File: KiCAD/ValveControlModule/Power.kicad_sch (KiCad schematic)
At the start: 1 part

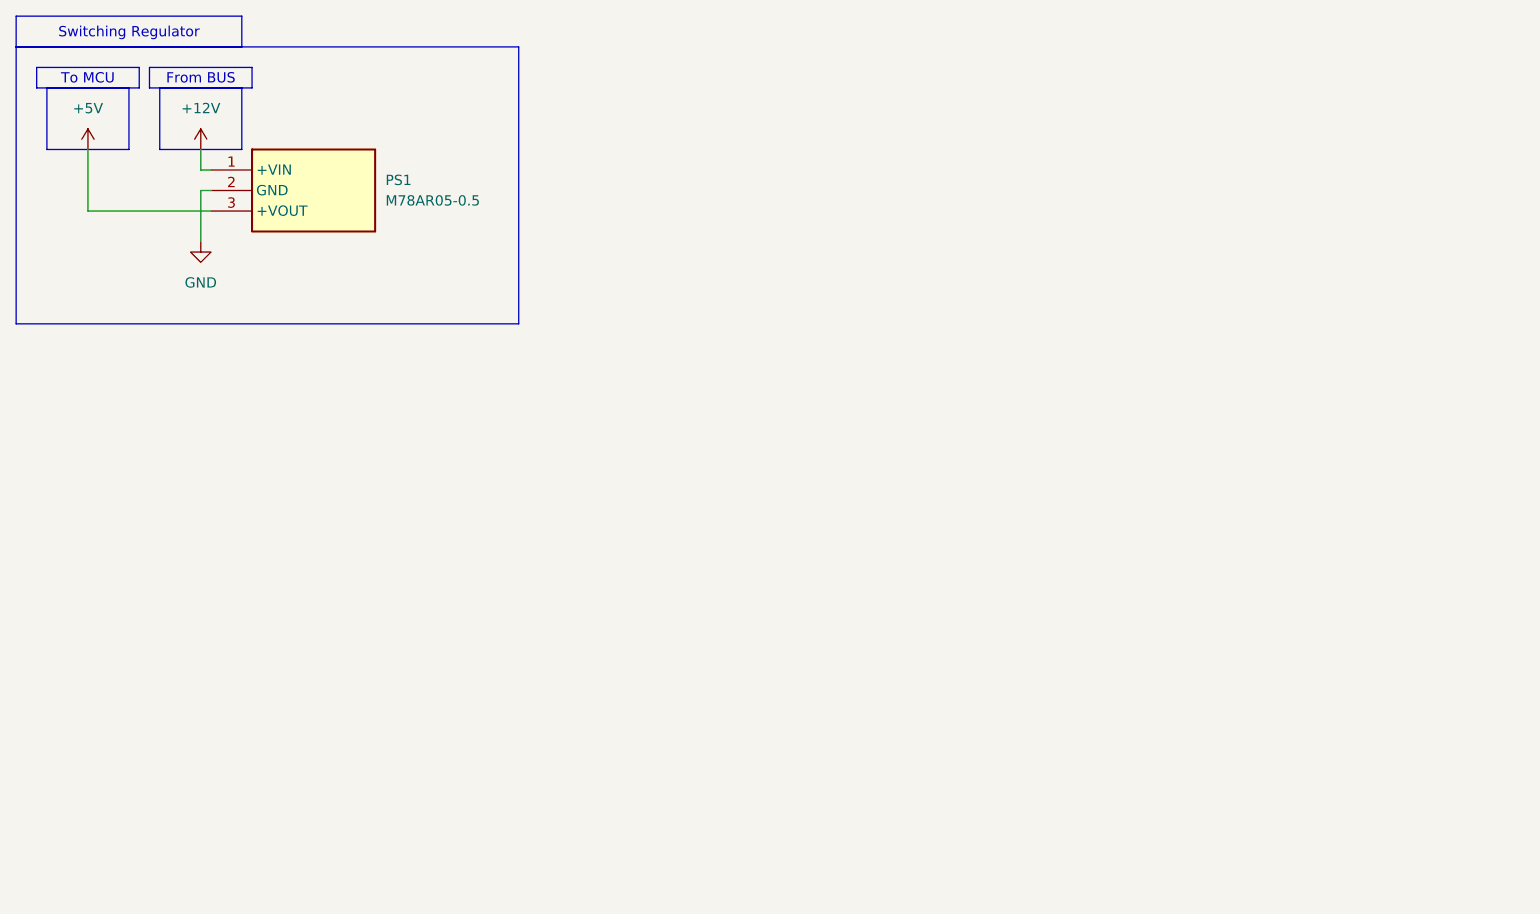
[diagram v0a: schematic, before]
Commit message: 電源，RS485の仕様を確定
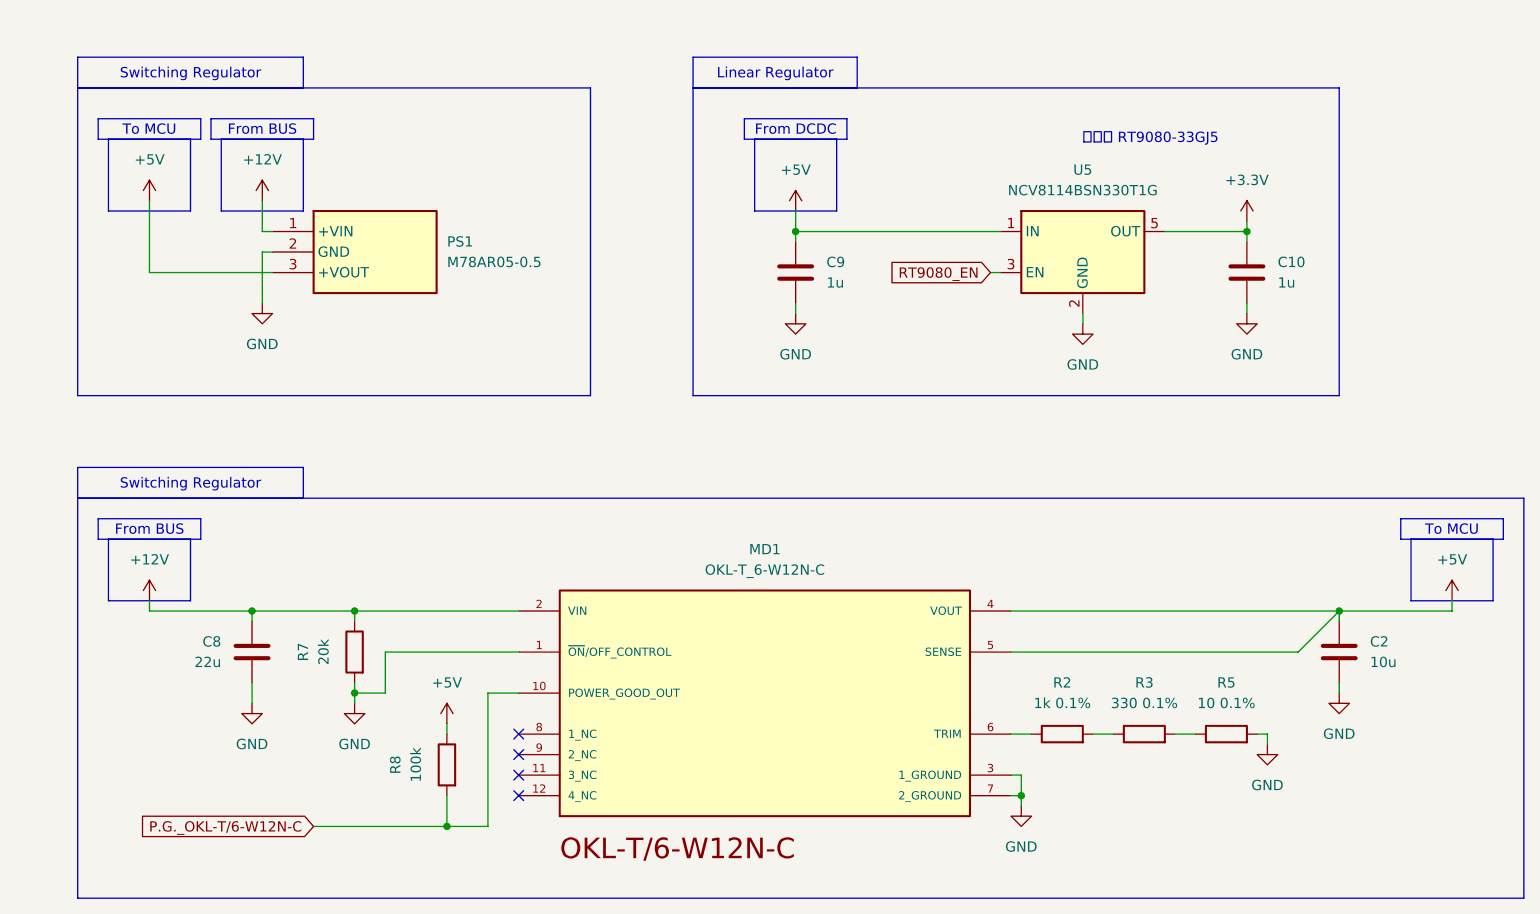
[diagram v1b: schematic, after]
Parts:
- added C10, C9: 1u, Capacitor_SMD:C_0603_1608Metric_Pad1.08x0.95mm_HandSolder, symbol Device:C
- added C2: 10u, Capacitor_SMD:C_0805_2012Metric_Pad1.18x1.45mm_HandSolder, symbol Device:C
- added C8: 22u, Capacitor_SMD:C_0805_2012Metric_Pad1.18x1.45mm_HandSolder, symbol Device:C
- added MD1: OKL-T_6-W12N-C, TSRP_IC:MURATA_OKL-T-6-W12N-C_0, symbol TSRP_IC:OKL-T_6-W12N-C
- added R2: 1k 0.1%, Resistor_SMD:R_0603_1608Metric_Pad0.98x0.95mm_HandSolder, symbol Device:R
- added R3: 330 0.1%, Resistor_SMD:R_0603_1608Metric_Pad0.98x0.95mm_HandSolder, symbol Device:R
- added R5: 10 0.1%, Resistor_SMD:R_0603_1608Metric_Pad0.98x0.95mm_HandSolder, symbol Device:R
- added R7: 20k, Resistor_SMD:R_0603_1608Metric_Pad0.98x0.95mm_HandSolder, symbol Device:R
- added R8: 100k, Resistor_SMD:R_0603_1608Metric_Pad0.98x0.95mm_HandSolder, symbol Device:R
- added U5: NCV8114BSN330T1G, Package_TO_SOT_SMD:TSOT-23-5, symbol Regulator_Linear:NCV8114BSN330T1G
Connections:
- net +12V: now also C8.1, MD1.2 (VIN), R7.1
- net +5V: now also C2.1, C9.1, MD1.4 (VOUT), MD1.5 (SENSE), R8.1, U5.1 (IN)
- net GND: now also C10.2, C2.2, C8.2, C9.2, MD1.1 (~{ON}/OFF_CONTROL), MD1.3 (1_GROUND), MD1.7 (2_GROUND), R5.2, R7.2, U5.2 (GND)
- new net: MD1.6 (TRIM), R2.1
- new net: R2.2, R3.1
- new net: R3.2, R5.1
- new net +3.3V: C10.1, U5.5 (OUT)
- new net P.G._OKL-T/6-W12N-C: MD1.10 (POWER_GOOD_OUT), R8.2
- new net RT9080_EN: U5.3 (EN)
- no-connect marks 0 -> 4
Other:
- note added: "本当は RT9080-33GJ5"
- moved on the sheet: PS1
